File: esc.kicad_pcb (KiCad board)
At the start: 4 copper layers, 40 x 45 mm, 212 parts, among them J1 Conn_01x01_Pin, J10 Conn_01x01_Pin, J11 Conn_01x01_Pin, J12 Conn_01x01_Pin, J2 Conn_01x01_Pin, J3 Conn_01x01_Pin, J4 Conn_01x01_Pin, J5 Conn_01x01_Pin, J6 Conn_01x01_Pin, J7 Conn_01x01_Pin, J8 Conn_01x01_Pin, J9 Conn_01x01_Pin, M1 STM32C011F6U6TR, M2 STM32C011F6U6TR, M3 STM32C011F6U6TR, M4 STM32C011F6U6TR, Q1 NP80N06D6, Q10 NP80N06D6, Q11 NP80N06D6, Q12 NP80N06D6, Q13 NP80N06D6, Q14 NP80N06D6, Q15 NP80N06D6, Q16 NP80N06D6, Q17 NP80N06D6, Q18 NP80N06D6, Q19 NP80N06D6, Q2 NP80N06D6, Q20 NP80N06D6, Q21 NP80N06D6, Q22 NP80N06D6, Q23 NP80N06D6, Q24 NP80N06D6, Q3 NP80N06D6, Q4 NP80N06D6, Q5 NP80N06D6, Q6 NP80N06D6, Q7 NP80N06D6, Q8 NP80N06D6, Q9 NP80N06D6

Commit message: ...
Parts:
- added REF**: Mounting_Wuerth_WA-SMSI-M1.6_H0.5mm_9774005633, Mounting_Wuerth:Mounting_Wuerth_WA-SMSI-M1.6_H0.5mm_9774005633, F.Cu at (246.0, 82.0)
- added REF**: Mounting_Wuerth_WA-SMSI-M1.6_H0.5mm_9774005633, Mounting_Wuerth:Mounting_Wuerth_WA-SMSI-M1.6_H0.5mm_9774005633, F.Cu at (246.0, 38.0)
- added REF**: Mounting_Wuerth_WA-SMSI-M1.6_H0.5mm_9774005633, Mounting_Wuerth:Mounting_Wuerth_WA-SMSI-M1.6_H0.5mm_9774005633, F.Cu at (214.0, 82.0)
- added REF**: Mounting_Wuerth_WA-SMSI-M1.6_H0.5mm_9774005633, Mounting_Wuerth:Mounting_Wuerth_WA-SMSI-M1.6_H0.5mm_9774005633, F.Cu at (214.0, 38.0)
- added REF**: Mounting_Wuerth_WA-SMSI-M1.6_H0.5mm_9774005633, Mounting_Wuerth:Mounting_Wuerth_WA-SMSI-M1.6_H0.5mm_9774005633, F.Cu at (252.0, 76.0)
- added REF**: Mounting_Wuerth_WA-SMSI-M1.6_H0.5mm_9774005633, Mounting_Wuerth:Mounting_Wuerth_WA-SMSI-M1.6_H0.5mm_9774005633, F.Cu at (208.0, 76.0)
- added REF**: Mounting_Wuerth_WA-SMSI-M1.6_H0.5mm_9774005633, Mounting_Wuerth:Mounting_Wuerth_WA-SMSI-M1.6_H0.5mm_9774005633, F.Cu at (208.0, 44.0)
- added REF**: Mounting_Wuerth_WA-SMSI-M1.6_H0.5mm_9774005633, Mounting_Wuerth:Mounting_Wuerth_WA-SMSI-M1.6_H0.5mm_9774005633, F.Cu at (252.0, 44.0)
- C10, C11, C12, C25, C26, C27, C40, C41, C42, C55, C56, C57: footprint easyeda2kicad:C0603 -> easyeda2kicad:C1206
- C63, C64, R81, R82, R83, R84, R85, R86, R87, R88, SWCLK_M1, SWCLK_M2, SWCLK_M3, SWCLK_M4, SWDIO_M1, SWDIO_M2, SWDIO_M3, SWDIO_M4: moved to B.Cu
- moved SWDIO_M4 50.9 mm to (224.0, 79.0), turned to 180 degrees
- moved SWCLK_M4 48.5 mm to (224.0, 76.9), turned to 180 degrees
- moved R82 48.2 mm to (225.8, 55.5), turned to 90 degrees
- moved R81 47.6 mm to (225.3, 52.0), turned to 180 degrees
- moved R83 47.3 mm to (225.3, 53.0), turned to 180 degrees
- moved R84 47.2 mm to (225.3, 54.0), turned to 180 degrees
- moved SWDIO_M2 47.2 mm to (221.0, 79.0), turned to 180 degrees
- moved C63 46.8 mm to (226.8, 55.6), turned to -90 degrees
- moved C29 46.6 mm to (213.2, 72.6), turned to 90 degrees
- moved SWCLK_M2 46.4 mm to (222.5, 79.0), turned to 180 degrees
- moved R34 45.5 mm to (214.2, 72.6), turned to -90 degrees
- moved C28 45.0 mm to (213.2, 66.6)
- moved R37 44.8 mm to (230.3, 48.5), turned to 0 degrees
- moved R33 44.5 mm to (215.2, 72.6), turned to 90 degrees
- moved C30 44.4 mm to (213.2, 78.6), turned to 90 degrees
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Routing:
- net 3V3: track 0.00 -> 135.3 mm, vias 0 -> 15
- net OUT3: track 29.4 -> 161.7 mm, vias 0 -> 72
- net OUT1: track 9.66 -> 106.7 mm, vias 0 -> 72
- net OUT2: track 8.85 -> 95.4 mm, vias 0 -> 72
- net GND: track 6.87 -> 91.3 mm, vias 166 -> 237
- net VIRTUAL_NEUTRAL_POINT: track 0.00 -> 47.7 mm
- net GLS3: track 16.2 -> 62.8 mm
- net GLS1: track 13.7 -> 51.1 mm
- net GLS2: track 11.8 -> 44.8 mm
- net GHS3: track 9.99 -> 39.1 mm
- net PHASE_B_M3: track 0.00 -> 28.0 mm, vias 0 -> 2
- net SWCLK_M2: track 0.00 -> 27.7 mm, vias 0 -> 2
- net PHASE_A_M1: track 0.04 -> 27.7 mm, vias 0 -> 2
- net SWCLK_M1: track 0.00 -> 27.5 mm, vias 0 -> 2
- net SWDIO_M2: track 0.00 -> 27.4 mm, vias 0 -> 2
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- added copper zone on B.Cu, net 3V3
- added copper zone on In2.Cu, net 3V3
- added copper zone on B.Cu, net B+
- added copper zone on B.Cu, net GND
- added copper zone on F.Cu, net OUT1
- added copper zone on F.Cu, net OUT2
- added copper zone on F.Cu, net OUT3
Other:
- board size 40 x 45 mm -> 48 x 49 mm

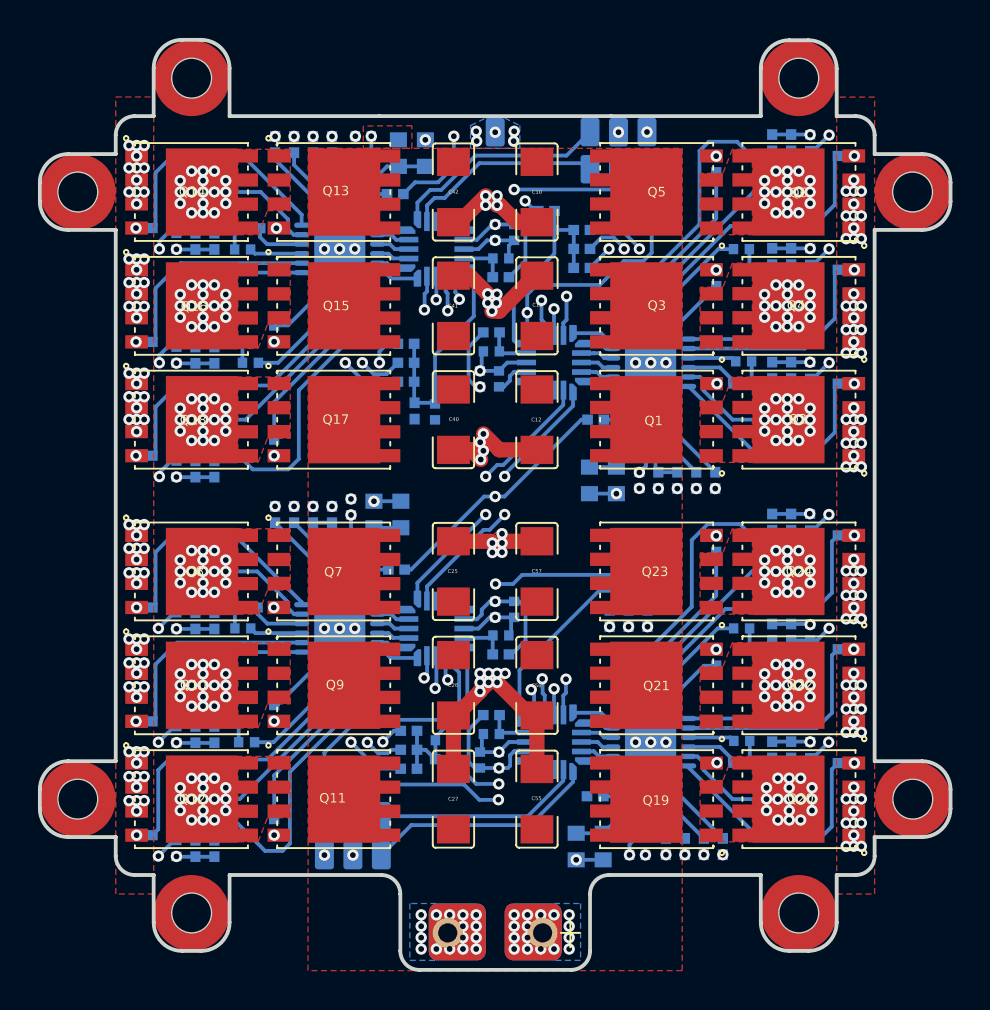
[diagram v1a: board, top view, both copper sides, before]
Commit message: new architecture ESC_V1.0 untested
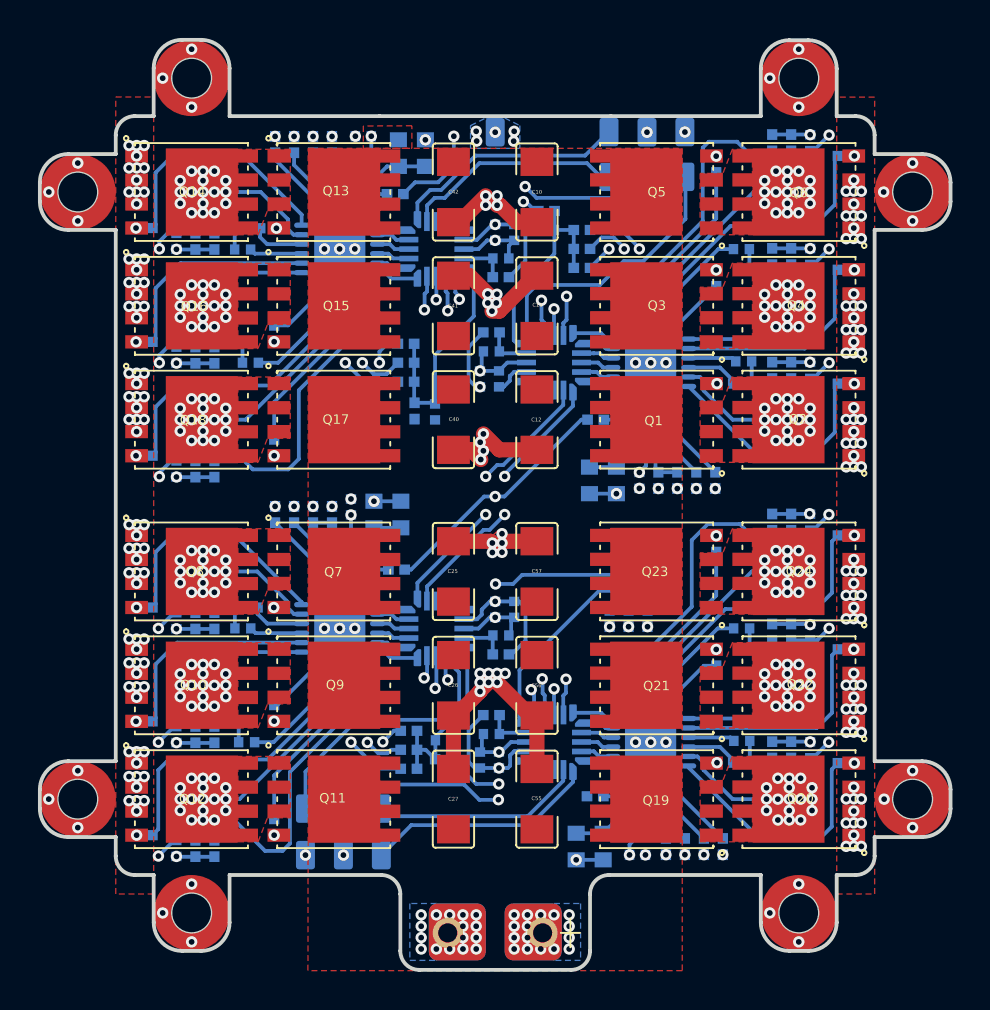
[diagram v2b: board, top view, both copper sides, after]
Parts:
- moved DShot_M1 2.04 mm to (240.0, 43.2)
- moved SWDIO_M1 2.00 mm to (240.0, 40.8)
- moved DShot_M3 1.55 mm to (238.0, 43.2)
- moved SWCLK_M1 1.50 mm to (238.0, 40.9)
- moved DShot_M2 1.08 mm to (220.0, 76.5)
- moved SWCLK_M3 1.08 mm to (236.0, 43.2)
- moved SWDIO_M2 1.00 mm to (220.0, 79.0)
- moved SWDIO_M3 1.00 mm to (236.0, 40.8)
- moved DShot_M4 0.64 mm to (222.0, 76.5)
- moved SWCLK_M2 0.50 mm to (222.0, 79.0)
- moved SWCLK_M4 0.40 mm to (224.0, 76.5)
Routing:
- net DShot_M3: track 16.5 -> 18.3 mm
- net 3V3: track 135.3 -> 137.0 mm
- net SWCLK_M3: track 10.5 -> 11.7 mm
- net SWDIO_M3: track 11.5 -> 12.5 mm
- net SWDIO_M1: track 27.2 -> 28.0 mm
- net SWCLK_M1: track 27.5 -> 28.1 mm
- net DShot_M1: track 14.2 -> 14.4 mm, vias 1 -> 0
- net GND: track 91.3 -> 91.4 mm, vias 237 -> 261
